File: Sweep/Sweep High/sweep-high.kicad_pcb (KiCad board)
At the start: 2 copper layers, 229.5 x 95.2 mm, 41 parts, among them J1 AudioJack4dpb, J2 AudioJack4dpb, SW10 SW_Push, SW11 SW_Push, SW11_r1 SW_Push, SW12 SW_Push, SW12_r1 SW_Push, SW13_r1 SW_Push, SW14 SW_Push, SW15 SW_Push, SW15_r1 SW_Push, SW16 SW_Push, SW16_r1 SW_Push, SW17 SW_Push, SW17_r1 SW_Push, SW18 SW_Push, SW18_r1 SW_Push, SW2 SW_Push, SW20 SW_Push, SW20_r1 SW_Push, SW21 SW_Push, SW21_r1 SW_Push, SW2_r1 SW_Push, SW3 SW_Push, SW3_r1 SW_Push, SW4 SW_Push, SW4_r1 SW_Push, SW5 SW_Push, SW5_r1 SW_Push, SW6 SW_Push, SW6_r1 SW_Push, SW7_r1 SW_Push, SW8 SW_Push, SW8_r1 SW_Push, SW9 SW_Push, SW9_r1 SW_Push, U1 ProMicro-kbd, U2 ProMicro-kbd

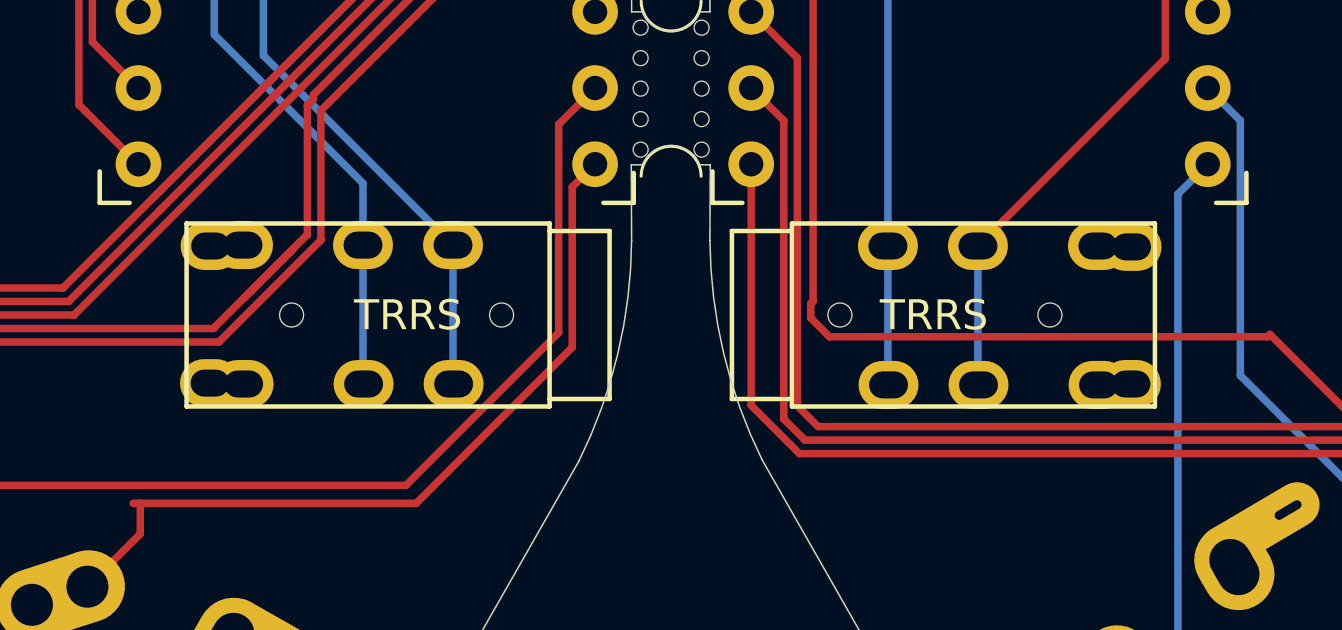
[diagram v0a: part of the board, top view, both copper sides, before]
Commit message: Updated TRRS to one side only
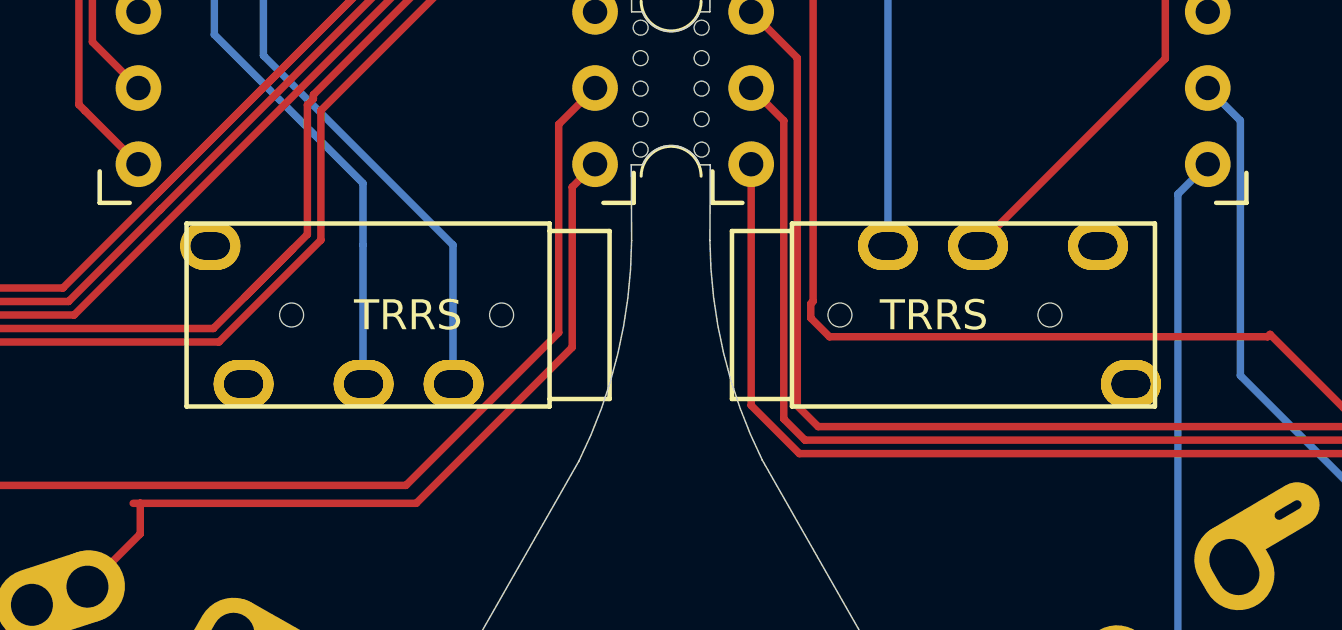
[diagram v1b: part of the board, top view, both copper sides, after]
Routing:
- net Switch18_r: track 36.0 -> 31.3 mm
- net vcc: track 62.7 -> 58.0 mm

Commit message: Add compatible gerber
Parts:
- removed the G*** at (215.8, 118.9)
- added G***: LOGO, silkscreens:unsafe_rust, B.Cu at (84.8, 92.1)
- added G***: LOGO, silkscreens:open_eyes, B.Cu at (218.9, 95.8)
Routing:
- net raw: track 0.00 -> 1.14 mm
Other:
- board text removed: "Face down"
